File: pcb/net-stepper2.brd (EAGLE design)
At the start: 41.9 x 90.2 mm, 42 parts, among them J1 MICRO-USB, J2 POWER_JACKPTH_LOCK, J3 ENCODER, J4 ENDSTOP2, J5 ENDSTOP1, J6 STEPER, Q1 600mA/40V, Q2 600mA/40V, U1 L6470, U2 CP2104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

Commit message: remapped pins
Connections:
- net ADC renamed SC_ADC
- net CSN renamed SC_CSN
- net DTR renamed ESP_DTR
- net OUT1A renamed SC_OUT1A
- net OUT1B renamed SC_OUT1B
- net OUT2A renamed SC_OUT2A
- net OUT2B renamed SC_OUT2B
- net PGRM renamed ESP_PGRM
- net RESET renamed ESP_RESET
- net RESETN renamed SC_RESETN
- net RTS renamed ESP_RTS
- net RX renamed ESP_RX
- net SCK renamed SC_SCK
- net SDI renamed SC_SDI
- net SDO renamed SC_SDO
- net TX renamed ESP_TX
- removed net BLUE: R12.2, U2.13, U5.7
- removed net DOWN: S1.P$1, U5.11
- removed net END_STOP_1: J5.2, U5.23
- removed net END_STOP_2: J4.2, U5.28
- removed net GREEN: R11.2, U2.14, U5.6
- removed net HOME: S4.P$1, U5.12
- removed net RED: R6.2, U5.8
- removed net STOP: S3.P$1, U5.14
- removed net UP: S2.P$1, U5.9
- new net BTN_DOWN: S1.P$1, U5.26
- new net BTN_HOME: S4.P$1, U5.16
- new net BTN_STOP: S3.P$1, U5.23
- new net BTN_UP: S2.P$1, U5.10, U5.28
- new net ENDS_1: J5.2, U5.8
- new net ENDS_2: J4.2, U5.9
- new net LED_BLUE: R12.2, U2.13, U5.13
- new net LED_GREEN: R11.2, U2.14, U5.12
- new net LED_RED: R6.2, U5.11
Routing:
- net BLUE: track 110.9 -> 0.00 mm, vias 2 -> 0
- net LED_BLUE: track 0.00 -> 108.7 mm, vias 0 -> 2
- net GREEN: track 105.0 -> 0.00 mm, vias 2 -> 0
- net LED_GREEN: track 0.00 -> 103.9 mm, vias 0 -> 2
- net DOWN: track 48.7 -> 0.00 mm
- net BTN_DOWN: track 0.00 -> 47.6 mm
- net STOP: track 44.6 -> 0.00 mm, vias 2 -> 0
- net BTN_STOP: track 0.00 -> 44.5 mm, vias 0 -> 2
- net HOME: track 41.3 -> 0.00 mm
- net BTN_HOME: track 0.00 -> 40.8 mm
- net UP: track 37.8 -> 0.00 mm
- net BTN_UP: track 0.00 -> 36.7 mm
- net RED: track 32.6 -> 0.00 mm, vias 2 -> 0
- net LED_RED: track 0.00 -> 30.1 mm, vias 0 -> 2
- net END_STOP_1: track 13.9 -> 0.00 mm, vias 1 -> 0
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
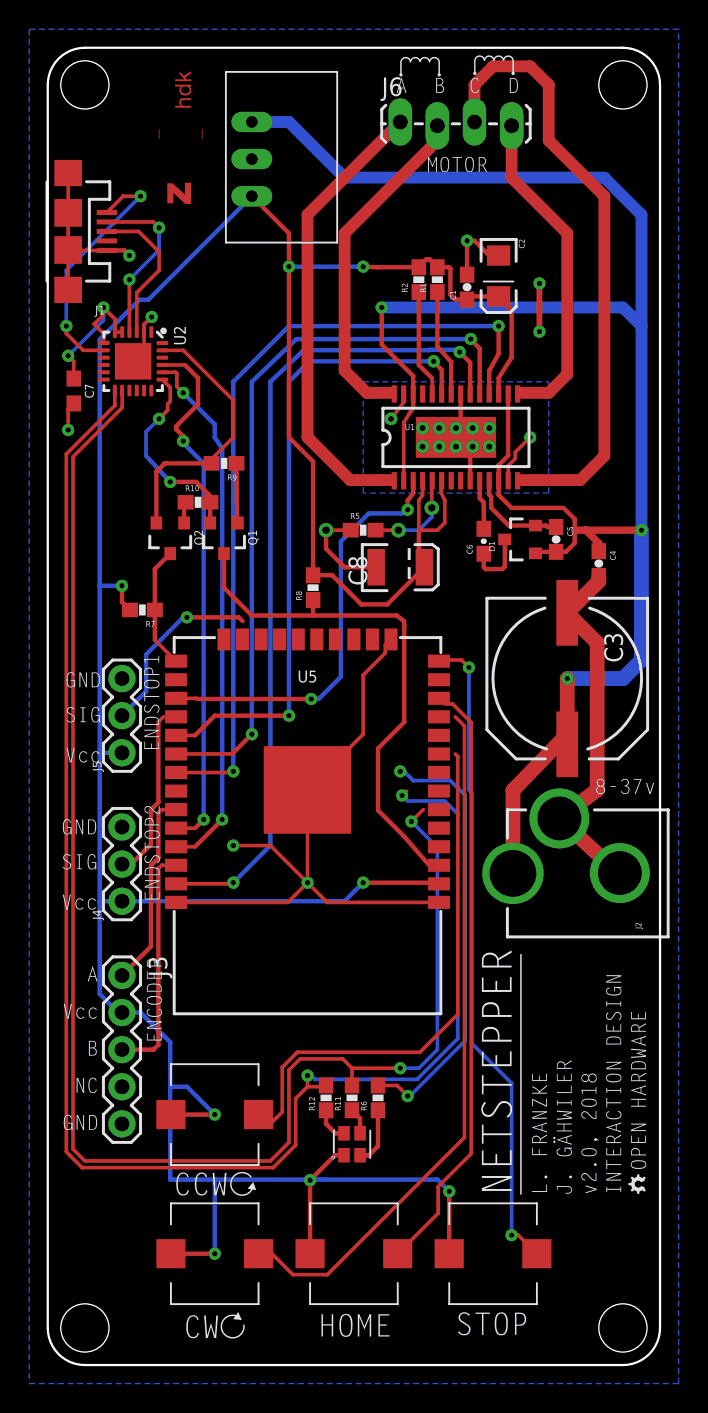
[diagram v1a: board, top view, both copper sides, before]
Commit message: prepared new routing
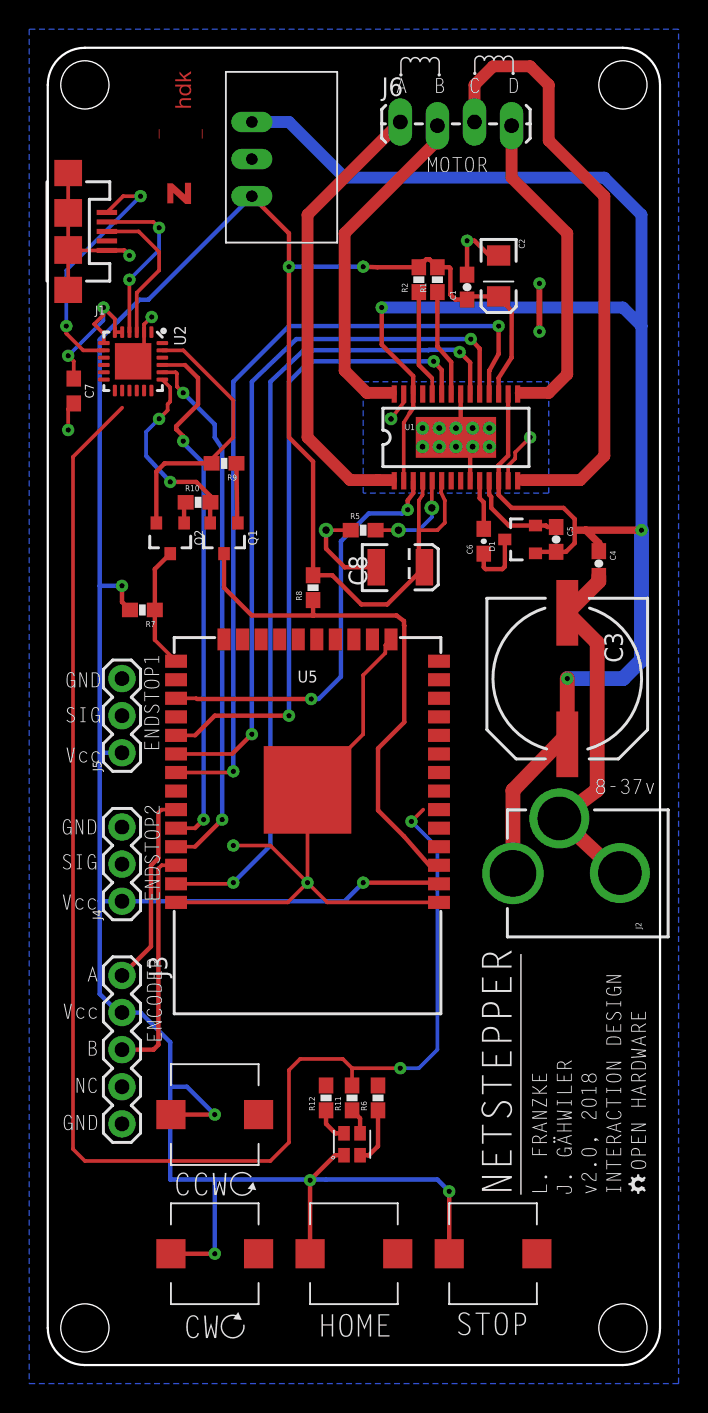
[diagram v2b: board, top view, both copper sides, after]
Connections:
- net BTN_UP: no longer U5.10
- net LED_BLUE: no longer U2.13
- net LED_GREEN: no longer U2.14
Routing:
- net LED_BLUE: track 108.7 -> 0.00 mm, vias 2 -> 0
- net BTN_DOWN: track 47.6 -> 0.00 mm
- net BTN_STOP: track 44.5 -> 0.00 mm, vias 2 -> 0
- net BTN_HOME: track 40.8 -> 0.00 mm
- net BTN_UP: track 36.7 -> 0.00 mm
- net LED_RED: track 30.1 -> 0.00 mm, vias 2 -> 0
- net ENDS_1: track 12.6 -> 0.00 mm, vias 1 -> 0
- net ENDS_2: track 11.7 -> 0.11 mm
- net LED_GREEN: track 103.9 -> 102.8 mm
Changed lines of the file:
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@@
 <signal name="BTN_DOWN">
 <contactref element="S1" pad="P$1"/>
-<wire x1="27.893" y1="44.37" x2="28.5242" y2="43.7388" width="0.254" layer="1"/>
-<wire x1="19.13385625" y1="6.1882" x2="16.77614375" y2="6.1882" width="0.254" layer="1"/>
-<wire x1="15.34434375" y1="7.62" x2="14.43" y2="7.62" width="0.254" layer="1"/>
-<wire x1="16.77614375" y1="6.1882" x2="15.34434375" y2="7.62" width="0.254" layer="1"/>
-<wire x1="28.5242" y1="15.57854375" x2="19.13385625" y2="6.1882" width="0.254" layer="1"/>
-<wire x1="28.5242" y1="43.7388" x2="28.5242" y2="15.57854375" width="0.254" layer="1"/>
 <contactref element="U5" pad="26"/>
-<wire x1="27.893" y1="44.37" x2="8.78" y2="46.91" width="0" layer="19" extent="1-1"/>
+<wire x1="14.43" y1="7.62" x2="8.78" y2="46.91" width="0" layer="19" extent="1-1"/>
 </signal>
 <signal name="BTN_UP">
 <contactref element="S2" pad="P$1"/>
-<wire x1="27.893" y1="41.83" x2="28.067" y2="41.656" width="0.254" layer="1"/>
-<wire x1="28.067" y1="41.656" x2="28.067" y2="24.003" width="0.254" layer="1"/>
-<wire x1="16.0528" y1="17.3228" x2="15.24" y2="16.51" width="0.254" layer="1"/>
-<wire x1="17.08261875" y1="21.4122" x2="16.0528" y2="20.38238125" width="0.254" layer="1"/>
-<wire x1="16.0528" y1="20.38238125" x2="16.0528" y2="17.3228" width="0.254" layer="1"/>
-<wire x1="28.067" y1="24.003" x2="25.4762" y2="21.4122" width="0.254" layer="1"/>
-<wire x1="25.4762" y1="21.4122" x2="17.08261875" y2="21.4122" width="0.254" layer="1"/>
-<wire x1="15.24" y1="16.51" x2="15.065" y2="16.51" width="0.254" layer="1"/>
-<wire x1="15.065" y1="16.51" x2="14.43" y2="17.145" width="0.254" layer="1"/>
-<contactref element="U5" pad="10"/>
 <contactref element="U5" pad="28"/>
-<wire x1="27.893" y1="41.83" x2="26.78" y2="43.1" width="0" layer="19" extent="1-1"/>
-<wire x1="8.78" y1="44.37" x2="26.78" y2="43.1" width="0" layer="19" extent="1-1"/>
+<wire x1="14.43" y1="17.145" x2="8.78" y2="44.37" width="0" layer="19" extent="1-1"/>
 </signal>
 <signal name="BTN_STOP">
 <contactref element="S3" pad="P$1"/>
-<wire x1="26.86" y1="48.26" x2="28.321" y2="48.26" width="0.254" layer="1"/>
-<wire x1="28.321" y1="48.26" x2="28.829" y2="47.752" width="0.254" layer="1"/>
-<via x="28.829" y="47.752" extent="1-16" drill="0.35"/>
-<wire x1="28.829" y1="47.752" x2="28.829" y2="39.38158125" width="0.254" layer="16"/>
-<wire x1="28.829" y1="39.38158125" x2="29.0322" y2="39.17838125" width="0.254" layer="16"/>
-<wire x1="29.0322" y1="39.17838125" x2="29.0322" y2="22.01245" width="0.254" layer="16"/>
-<wire x1="29.0322" y1="22.01245" x2="31.75" y2="19.29465" width="0.254" layer="16"/>
-<wire x1="31.75" y1="19.29465" x2="31.75" y2="8.89" width="0.254" layer="16"/>
-<via x="31.75" y="8.89" extent="1-16" drill="0.35"/>
-<wire x1="31.75" y1="8.89" x2="32.21" y2="8.89" width="0.254" layer="1"/>
-<wire x1="32.21" y1="8.89" x2="33.48" y2="7.62" width="0.254" layer="1"/>
 <contactref element="U5" pad="23"/>
-<wire x1="26.86" y1="48.26" x2="13.335" y2="49.67" width="0" layer="19" extent="1-1"/>
+<wire x1="33.48" y1="7.62" x2="13.335" y2="49.67" width="0" layer="19" extent="1-1"/>
 </signal>
 <signal name="BTN_HOME">
 <contactref element="S4" pad="P$1"/>
-<wire x1="27.1682" y1="45.2518" x2="27.70885625" y2="45.2518" width="0.254" layer="1"/>
-<wire x1="27.70885625" y1="45.2518" x2="28.9814" y2="43.97925625" width="0.254" layer="1"/>
-<wire x1="26.7208" y1="10.3858" x2="23.955" y2="7.62" width="0.254" layer="1"/>
-<wire x1="28.9814" y1="14.465075" x2="26.7208" y2="12.204475" width="0.254" layer="1"/>
-<wire x1="26.7208" y1="12.204475" x2="26.7208" y2="10.3858" width="0.254" layer="1"/>
-<wire x1="28.9814" y1="43.97925625" x2="28.9814" y2="14.465075" width="0.254" layer="1"/>
 <contactref element="U5" pad="16"/>
-<wire x1="27.1682" y1="45.2518" x2="22.225" y2="49.67" width="0" layer="19" extent="1-1"/>
+<wire x1="23.955" y1="7.62" x2="22.225" y2="49.67" width="0" layer="19" extent="1-1"/>
 </signal>
 <signal name="VBUS">
@@
 <signal name="LED_RED">
 <contactref element="R6" pad="2"/>
-<wire x1="24.431" y1="40.56" x2="24.384" y2="40.513" width="0.254" layer="1"/>
-<wire x1="24.384" y1="40.513" x2="24.337" y2="40.56" width="0.254" layer="1"/>
-<wire x1="24.257" y1="40.64" x2="24.13" y2="40.64" width="0.254" layer="1"/>
-<via x="24.13" y="40.64" extent="1-16" drill="0.35"/>
-<wire x1="24.13" y1="40.64" x2="24.384" y2="40.64" width="0.254" layer="16"/>
-<wire x1="24.384" y1="40.64" x2="25.019" y2="40.005" width="0.254" layer="16"/>
-<wire x1="25.019" y1="40.005" x2="27.559" y2="40.005" width="0.254" layer="16"/>
-<wire x1="27.559" y1="40.005" x2="28.575" y2="38.989" width="0.254" layer="16"/>
-<wire x1="28.575" y1="38.989" x2="28.575" y2="22.20183125" width="0.254" layer="16"/>
-<wire x1="28.575" y1="22.20183125" x2="24.78816875" y2="18.415" width="0.254" layer="16"/>
-<via x="24.638" y="18.415" extent="1-16" drill="0.35"/>
-<wire x1="24.638" y1="18.415" x2="23.915" y2="19.138" width="0.254" layer="1"/>
-<wire x1="23.915" y1="19.138" x2="22.606" y2="19.138" width="0.254" layer="1"/>
-<wire x1="24.78816875" y1="18.415" x2="24.638" y2="18.415" width="0.254" layer="16"/>
-<wire x1="24.337" y1="40.56" x2="24.257" y2="40.64" width="0.254" layer="1"/>
 <contactref element="U5" pad="11"/>
-<wire x1="24.384" y1="40.64" x2="26.78" y2="44.37" width="0" layer="19" extent="1-16"/>
+<wire x1="22.606" y1="19.138" x2="26.78" y2="44.37" width="0" layer="19" extent="1-1"/>
 </signal>
 <signal name="LED_GREEN">
@@
 <wire x1="24.892" y1="37.211" x2="25.701" y2="38.02" width="0.254" layer="1"/>
 <wire x1="25.39999375" y1="20.32" x2="26.67" y2="21.59000625" width="0.254" layer="16"/>
-<contactref element="U2" pad="14"/>
-<wire x1="5.092" y1="66.707" x2="5.092" y2="65.53241875" width="0.254" layer="1"/>
 <wire x1="5.092" y1="65.53241875" x2="1.7272" y2="62.16761875" width="0.254" layer="1"/>
 <contactref element="U5" pad="12"/>
@@
 <signal name="LED_BLUE">
 <contactref element="R12" pad="2"/>
-<wire x1="4.592" y1="65.679" x2="1.27" y2="62.357" width="0.254" layer="1"/>
-<wire x1="1.27" y1="62.357" x2="1.27" y2="14.605" width="0.254" layer="1"/>
-<wire x1="1.27" y1="14.605" x2="1.51241875" y2="14.351" width="0.254" layer="1"/>
-<wire x1="1.51241875" y1="14.351" x2="2.35061875" y2="13.5128" width="0.254" layer="1"/>
-<wire x1="2.35061875" y1="13.5128" x2="15.42938125" y2="13.5128" width="0.254" layer="1"/>
-<wire x1="15.42938125" y1="13.5128" x2="16.9672" y2="15.05061875" width="0.254" layer="1"/>
-<wire x1="16.9672" y1="18.2372" x2="17.78" y2="19.05" width="0.254" layer="1"/>
-<wire x1="17.78" y1="19.05" x2="18.962" y2="19.05" width="0.254" layer="1"/>
-<wire x1="18.962" y1="19.05" x2="19.05" y2="19.138" width="0.254" layer="1"/>
-<wire x1="16.9672" y1="15.05061875" x2="16.9672" y2="18.2372" width="0.254" layer="1"/>
-<via x="24.257" y="38.989" extent="1-16" drill="0.35"/>
-<wire x1="24.257" y1="38.989" x2="24.638" y2="38.608" width="0.254" layer="16"/>
-<wire x1="27.178" y1="38.608" x2="28.067" y2="37.719" width="0.254" layer="16"/>
-<wire x1="28.067" y1="37.719" x2="28.067" y2="22.34041875" width="0.254" layer="16"/>
-<wire x1="24.558" y1="39.29" x2="24.257" y2="38.989" width="0.254" layer="1"/>
-<wire x1="24.638" y1="38.608" x2="27.178" y2="38.608" width="0.254" layer="16"/>
-<wire x1="18.288" y1="19.558" x2="17.78" y2="20.066" width="0.254" layer="16"/>
-<wire x1="17.78" y1="20.066" x2="17.78" y2="19.812" width="0.254" layer="16"/>
-<via x="17.78" y="19.812" extent="1-16" drill="0.35"/>
-<wire x1="17.78" y1="19.812" x2="17.78" y2="19.05" width="0.254" layer="1"/>
-<wire x1="28.067" y1="22.34041875" x2="25.28458125" y2="19.558" width="0.254" layer="16"/>
-<wire x1="25.28458125" y1="19.558" x2="18.288" y2="19.558" width="0.254" layer="16"/>
-<contactref element="U2" pad="13"/>
-<wire x1="4.592" y1="66.707" x2="4.592" y2="65.679" width="0.254" layer="1"/>
 <contactref element="U5" pad="13"/>
-<wire x1="24.558" y1="39.29" x2="26.78" y2="46.91" width="0" layer="19" extent="1-1"/>
+<wire x1="19.05" y1="19.138" x2="26.78" y2="46.91" width="0" layer="19" extent="1-1"/>
 </signal>
 <signal name="N$11">
@@
 <contactref element="J4" pad="2"/>
 <wire x1="5.16" y1="34.21" x2="5.08" y2="34.29" width="0.3048" layer="1"/>
-<wire x1="5.08" y1="34.29" x2="5.715" y2="34.29" width="0.3048" layer="1"/>
-<wire x1="7.0648" y1="35.6398" x2="7.0648" y2="38.009225" width="0.3048" layer="1"/>
-<wire x1="7.0648" y1="38.009225" x2="7.5728" y2="38.517225" width="0.3048" layer="1"/>
-<wire x1="5.715" y1="34.29" x2="7.0648" y2="35.6398" width="0.3048" layer="1"/>
-<wire x1="7.5728" y1="44.0218" x2="7.5728" y2="38.517225" width="0.3048" layer="1"/>
-<wire x1="7.921" y1="44.37" x2="7.5728" y2="44.0218" width="0.254" layer="1"/>
-<wire x1="7.921" y1="44.37" x2="26.78" y2="41.83" width="0" layer="19" extent="1-1"/>
+<wire x1="5.16" y1="34.21" x2="26.78" y2="41.83" width="0" layer="19" extent="1-1"/>
 </signal>
 <signal name="ENDS_1">
 <contactref element="U5" pad="8"/>
 <contactref element="J5" pad="2"/>
-<wire x1="13.335" y1="50.927" x2="13.081" y2="51.181" width="0.3048" layer="1"/>
-<wire x1="13.081" y1="51.181" x2="9.525" y2="51.181" width="0.3048" layer="1"/>
-<wire x1="6.731" y1="46.101" x2="6.731" y2="48.641" width="0.3048" layer="16"/>
-<wire x1="9.271" y1="51.181" x2="9.525" y2="51.181" width="0.3048" layer="16"/>
-<via x="9.525" y="51.181" extent="1-16" drill="0.35"/>
-<wire x1="5.08" y1="44.45" x2="6.731" y2="46.101" width="0.3048" layer="16"/>
-<wire x1="6.731" y1="48.641" x2="9.271" y2="51.181" width="0.3048" layer="16"/>
-<wire x1="13.335" y1="50.927" x2="26.78" y2="40.56" width="0" layer="19" extent="1-1"/>
+<wire x1="5.08" y1="44.45" x2="26.78" y2="40.56" width="0" layer="19" extent="1-1"/>
 </signal>
 </signals>

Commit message: Missing routing fixed
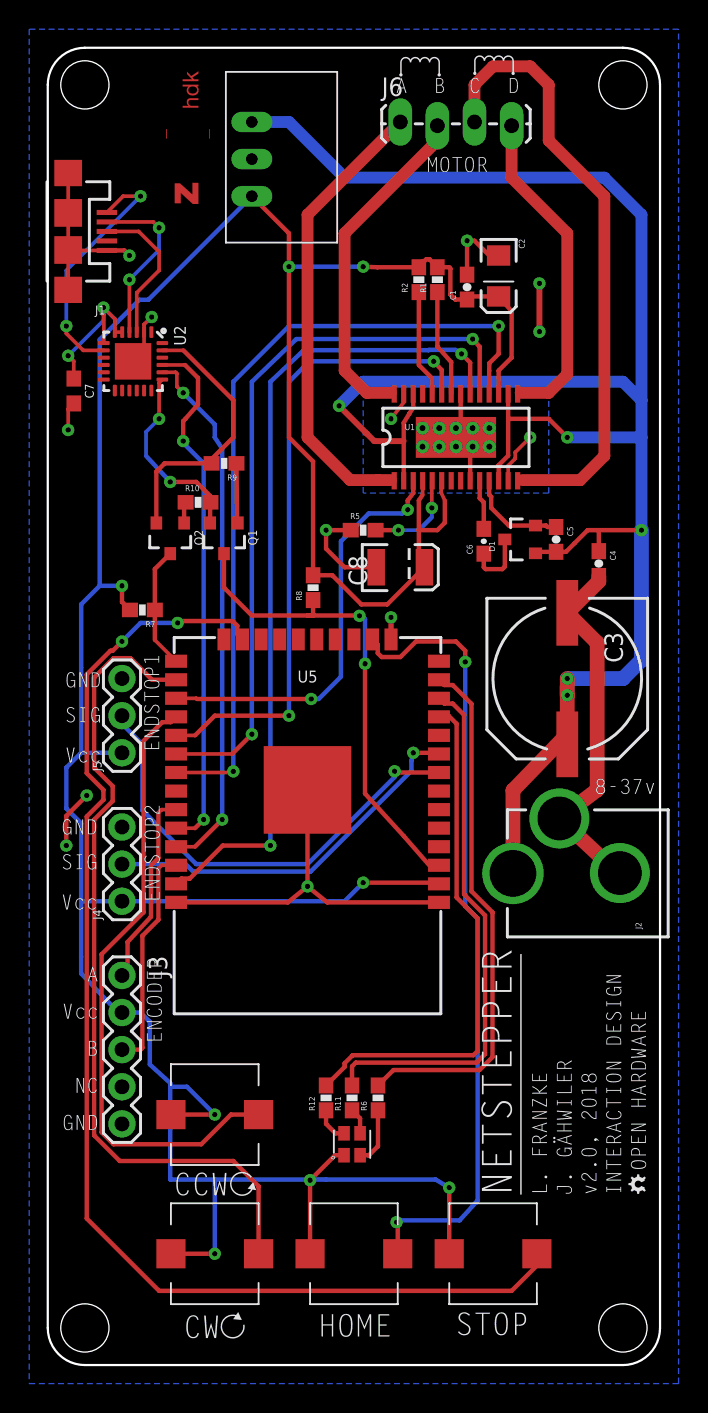
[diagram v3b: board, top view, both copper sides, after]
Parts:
- moved A1 0.51 mm to (8.13, 78.7)
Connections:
- net LED_BLUE: now also U5.11; no longer U5.13
- net LED_RED: now also U5.13; no longer U5.11
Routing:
- net BTN_STOP: track 0.00 -> 85.6 mm, vias 0 -> 2
- net LED_GREEN: track 102.8 -> 36.8 mm, vias 2 -> 0
- net BTN_DOWN: track 0.00 -> 56.5 mm
- net BTN_HOME: track 0.00 -> 54.3 mm, vias 0 -> 2
- net BTN_UP: track 0.00 -> 42.8 mm
- net LED_RED: track 0.00 -> 36.9 mm
- net LED_BLUE: track 0.00 -> 36.0 mm
- net ENDS_1: track 0.00 -> 32.0 mm, vias 0 -> 1
- net ENDS_2: track 0.11 -> 26.0 mm, vias 0 -> 1
- net GND: track 115.3 -> 105.2 mm, vias 21 -> 23
- net 3.3V: track 237.0 -> 242.1 mm
- net VS: track 136.2 -> 140.2 mm, vias 3 -> 5
- net ESP_RESET: track 36.1 -> 33.5 mm, vias 0 -> 2
- net ENC_B: track 16.0 -> 15.5 mm
